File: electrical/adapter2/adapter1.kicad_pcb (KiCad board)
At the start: 2 copper layers, 56.8 x 90 mm, 38 parts, among them J2 Conn_01x08_Pin, J3 0.5 mm, 24P, J4 0.5 mm, 24P, Q1 BSS138, Q2 AO3401A, Q3 S8050 SMD

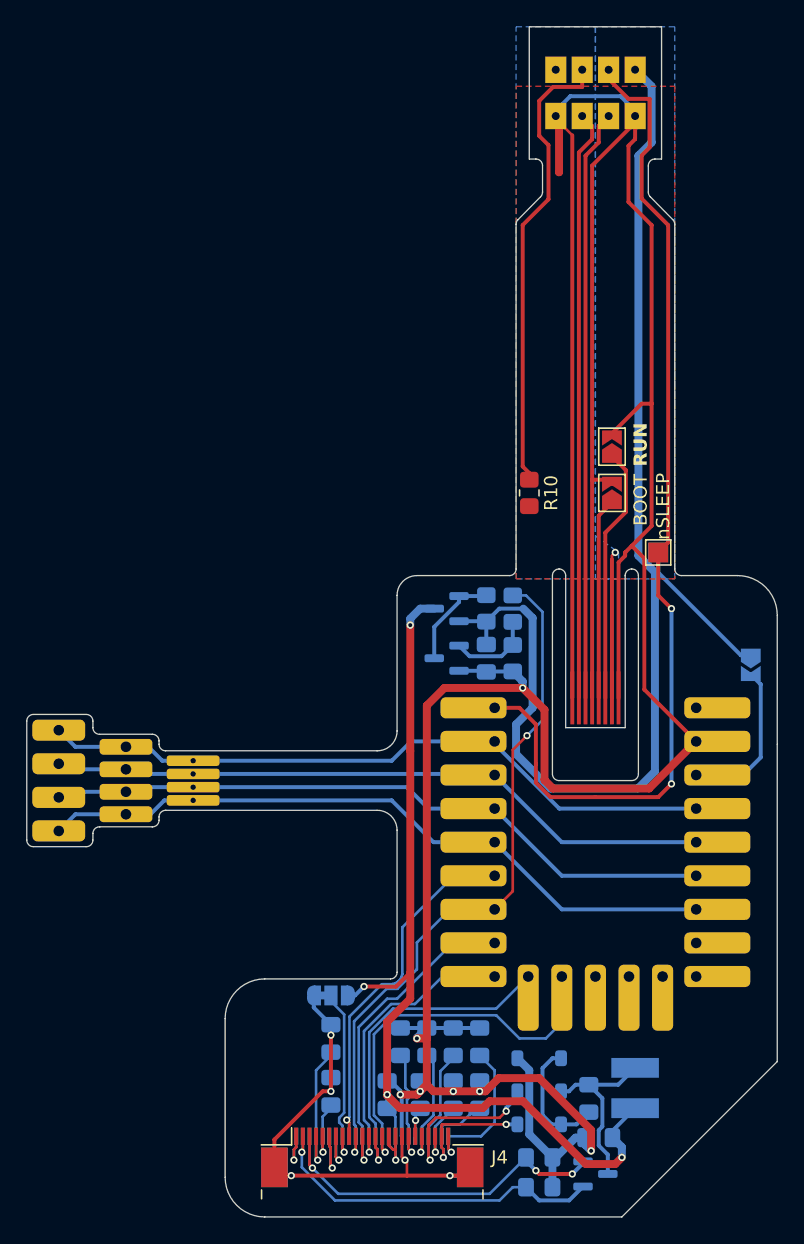
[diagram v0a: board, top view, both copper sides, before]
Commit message: remove hard corners from tracks
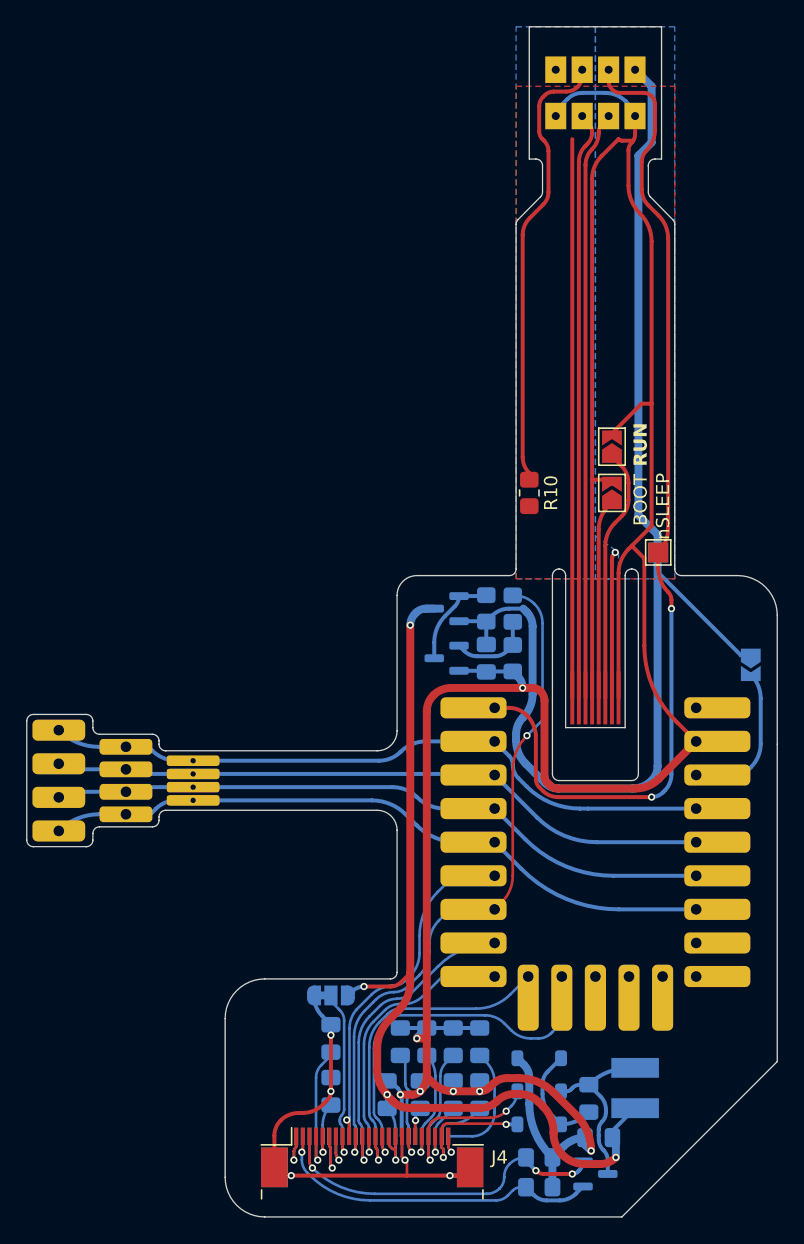
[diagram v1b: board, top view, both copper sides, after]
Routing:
- net GND: track 322.0 -> 314.3 mm
- net Net-(J5-Pin_4): track 52.6 -> 51.4 mm
- net /BUSY: track 28.0 -> 29.1 mm
- net Net-(D1-A): track 9.43 -> 8.34 mm
- net +5V: track 11.1 -> 12.2 mm
- net Net-(J1-BOARD_ID): track 34.9 -> 34.2 mm
- net Net-(J5-Pin_3): track 51.3 -> 50.6 mm
- net /RST: track 53.3 -> 52.6 mm
- net Net-(J3-Pin_5): track 9.14 -> 9.78 mm
- net /DC: track 25.0 -> 24.4 mm
- net /GDR: track 27.2 -> 26.5 mm
- net /DIN: track 30.1 -> 29.5 mm
